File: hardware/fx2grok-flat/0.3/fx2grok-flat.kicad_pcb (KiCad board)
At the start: 4 copper layers, 35 x 16 mm, 38 parts, among them IC1 CY7C68013A-56, J1 Conn, P1 pkl_USB_OTG, U1 3.3V, U2 USBLC6-2, U3 IP425x-4-TTL, U4 IP425x-4-TTL, U5 24LC00, U6 IP425x-4-TTL, X1 24MHz

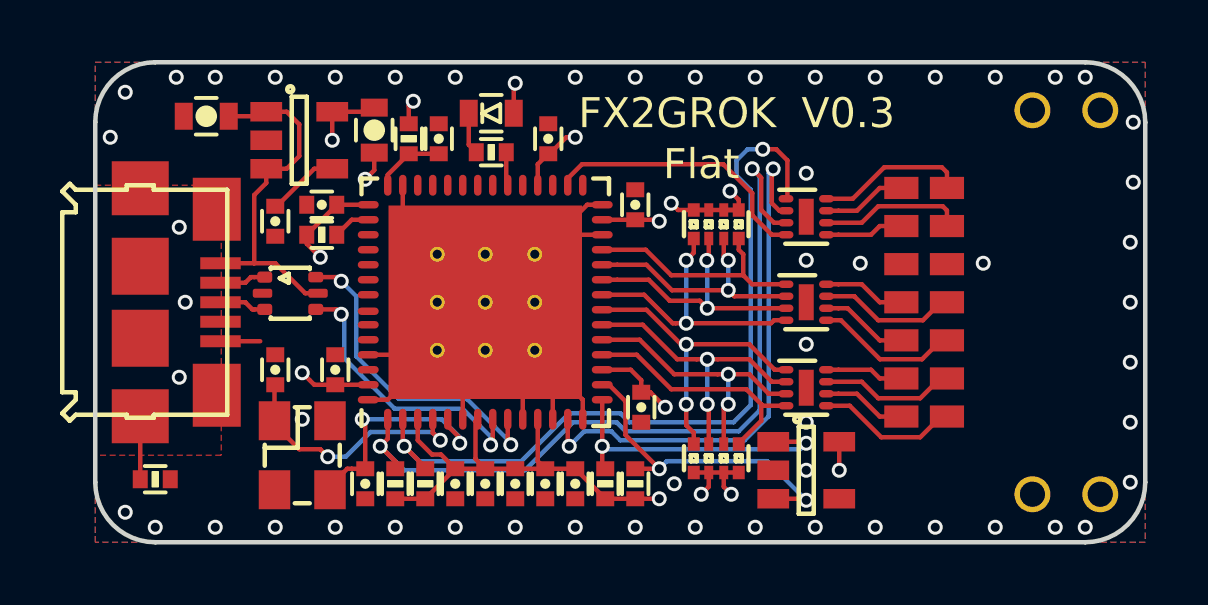
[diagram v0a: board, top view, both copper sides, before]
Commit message: Added GND via and fixed a DRC error.
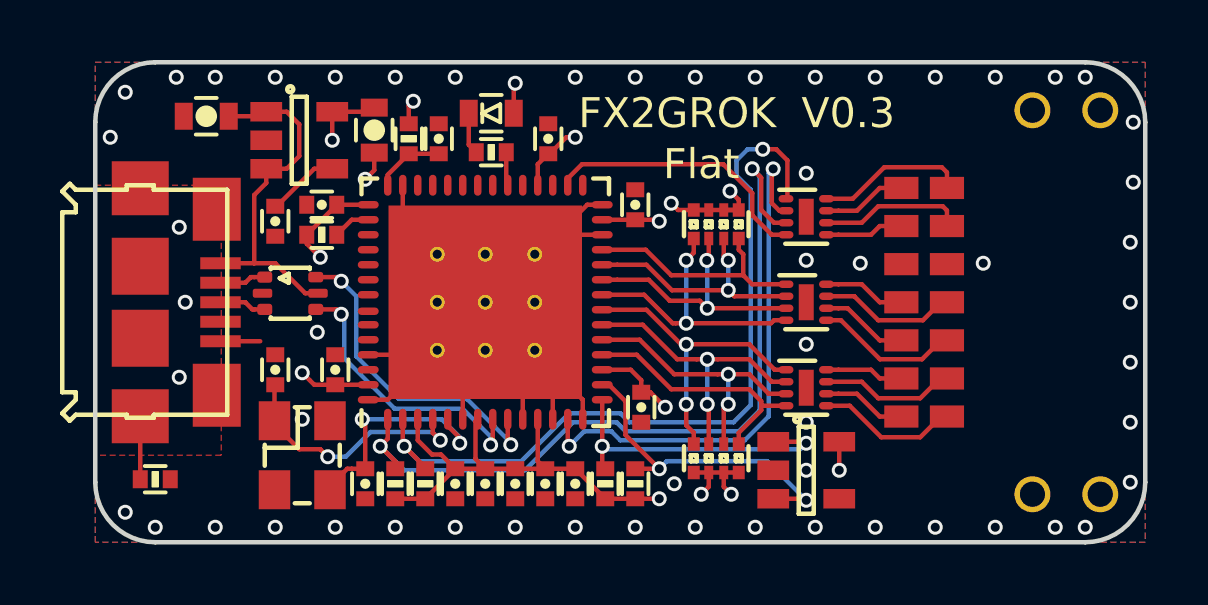
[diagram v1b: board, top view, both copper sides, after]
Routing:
- net GND: vias 52 -> 53
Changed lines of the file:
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@@
     (thickness 1.6)
     (drawings 47)
-    (tracks 479)
+    (tracks 480)
     (zones 0)
     (modules 38)
@@
   (via (at 45.7 36.6) (size 0.5) (drill 0.3) (layers F.Cu B.Cu) (net 8))
   (segment (start 45.65 36.55) (end 45.7 36.6) (width 0.15) (layer F.Cu) (net 8))
-  (segment (start 44.2 33.45) (end 44.2 33.4) (width 0.15) (layer F.Cu) (net 9))
-  (segment (start 44.2 33.4) (end 43.7 32.9) (width 0.15) (layer F.Cu) (net 9))
-  (segment (start 43.7 32.9) (end 41.2 32.9) (width 0.15) (layer F.Cu) (net 9))
-  (segment (start 41.2 32.9) (end 40.05 31.75) (width 0.15) (layer F.Cu) (net 9))
-  (segment (start 40.05 31.75) (end 38.9 31.75) (width 0.15) (layer F.Cu) (net 9))
   (segment (start 45.025 33.45) (end 44.2 33.45) (width 0.15) (layer F.Cu) (net 9))
-  (segment (start 43.45 34.725) (end 43.45 34.7) (width 0.15) (layer F.Cu) (net 9))
-  (segment (start 43.45 34.7) (end 44.2 33.95) (width 0.15) (layer F.Cu) (net 9))
-  (segment (start 44.2 33.95) (end 44.2 33.45) (width 0.15) (layer F.Cu) (net 9))
   (segment (start 42.95 33.55) (end 43.1 33.4) (width 0.15) (layer F.Cu) (net 10))
   (segment (start 42.95 34.725) (end 42.95 33.55) (width 0.15) (layer F.Cu) (net 10))
@@
   (via (at 23 23) (size 0.5) (drill 0.3) (layers F.Cu B.Cu) (net 2))
   (via (at 22.5 24.5) (size 0.5) (drill 0.3) (layers F.Cu B.Cu) (net 2))
+  (via (at 29.4 31) (size 0.5) (drill 0.3) (layers F.Cu B.Cu) (net 2))
   (segment (start 29 29.7) (end 29.425 29.7) (width 0.15) (layer F.Cu) (net 3))
   (segment (start 28 28.7) (end 29 29.7) (width 0.15) (layer F.Cu) (net 3))
@@
   (segment (start 39.675999 33.300999) (end 39.675999 34.426005) (width 0.15) (layer F.Cu) (net 8))
   (segment (start 44.398022 35.298022) (end 41.051972 35.298022) (width 0.15) (layer B.Cu) (net 8))
+  (segment (start 44.2 33.6) (end 44.2 33.45) (width 0.15) (layer F.Cu) (net 9))
+  (segment (start 43.45 34.35) (end 44.2 33.6) (width 0.15) (layer F.Cu) (net 9))
+  (segment (start 43.45 34.725) (end 43.45 34.35) (width 0.15) (layer F.Cu) (net 9))
+  (segment (start 40.05 31.75) (end 38.9 31.75) (width 0.15) (layer F.Cu) (net 9))
+  (segment (start 44.2 33.45) (end 44.2 33.3) (width 0.15) (layer F.Cu) (net 9))
+  (segment (start 44.2 33.3) (end 43.8 32.9) (width 0.15) (layer F.Cu) (net 9))
+  (segment (start 43.8 32.9) (end 41.2 32.9) (width 0.15) (layer F.Cu) (net 9))
+  (segment (start 41.2 32.9) (end 40.05 31.75) (width 0.15) (layer F.Cu) (net 9))
   (segment (start 46.775 33.05) (end 46.375 33.05) (width 0.15) (layer F.Cu) (net 19))
   (segment (start 47.39 33.05) (end 46.775 33.05) (width 0.15) (layer F.Cu) (net 19))

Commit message: Left a note that the next revision has to get roundrect pads.
Totally forgot to change them... and I already ordered the boards so it
is too late for the current revision. :(
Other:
- board text added: "Note: Make sure next revision uses roundrect pads! :)"
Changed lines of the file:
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@@
   (general
     (thickness 1.6)
-    (drawings 47)
+    (drawings 48)
     (tracks 480)
     (zones 0)
@@
     (46 B.CrtYd user)
     (47 F.CrtYd user)
-    (48 B.Fab user hide)
+    (48 B.Fab user)
     (49 F.Fab user)
   )
@@
       (effects (font (size 1 1) (thickness 0.15)) (justify mirror))
     )
-    (fp_text value 1b2_Logo_SilkS_10mm (at 0 6.35 90) (layer B.Fab)
+    (fp_text value 1b2_Logo_SilkS_10mm (at 0 6.35 90) (layer B.Fab) hide
       (effects (font (size 1 1) (thickness 0.15)) (justify mirror))
     )
@@
     )
   )
+  (gr_text "Note: Make sure next revision\nuses roundrect pads! :)" (at 40 43) (layer F.Fab)
+    (effects (font (size 1 1) (thickness 0.2)))
+  )
   (gr_text "T\n2" (at 55.5 26.1 90) (layer B.SilkS)
